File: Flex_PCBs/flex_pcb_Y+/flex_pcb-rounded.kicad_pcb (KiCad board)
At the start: 2 copper layers, 60 x 43.9 mm, 3 parts, among them J1 Conn_01x08_Male, J2 Conn_01x08_Male

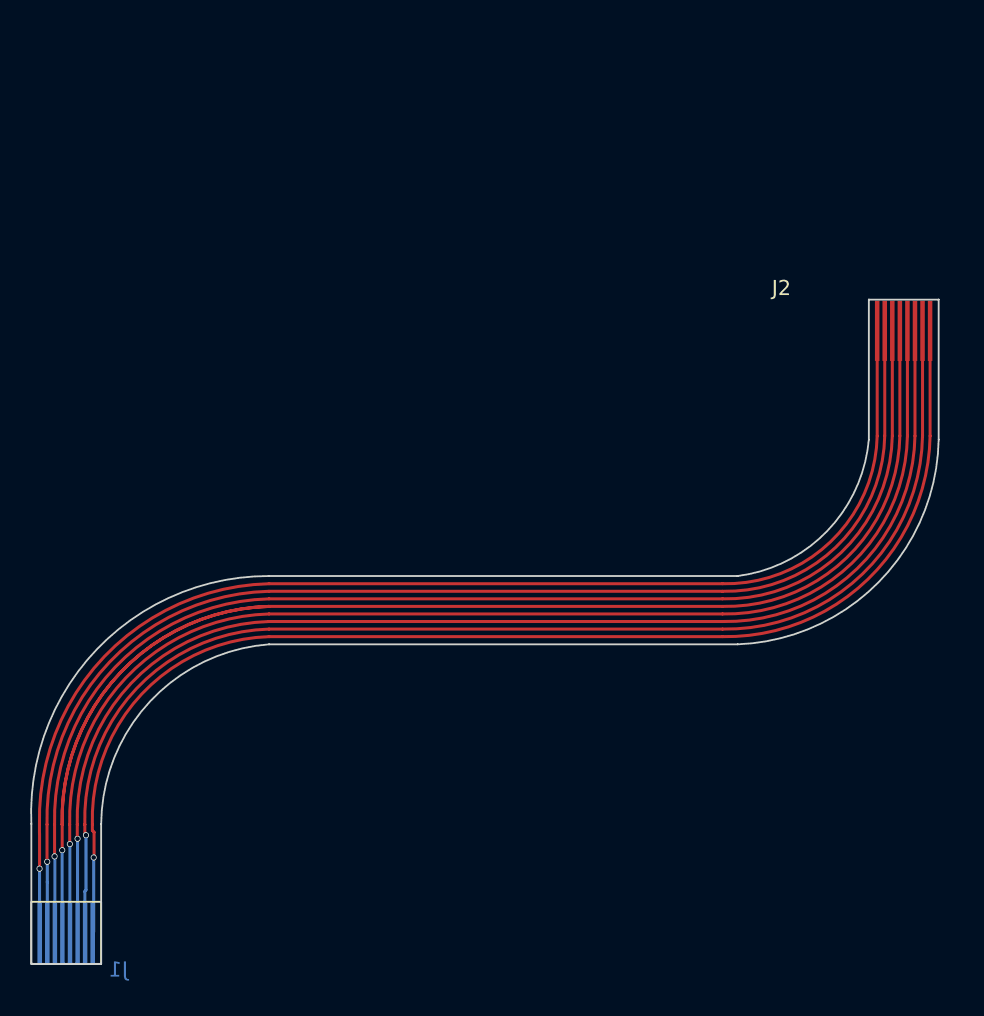
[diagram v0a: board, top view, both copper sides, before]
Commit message: Added small modifications to the existing flex PCBs plus the new ones: Y- and X-.
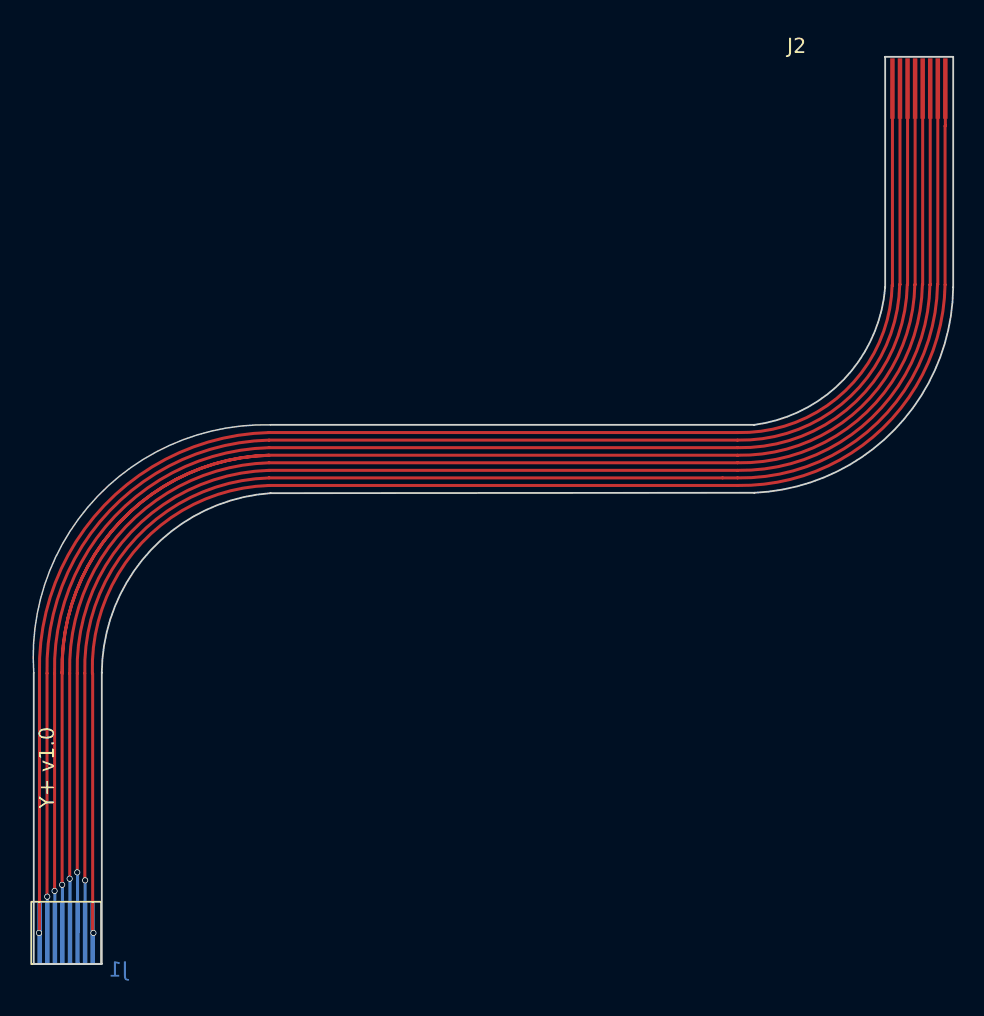
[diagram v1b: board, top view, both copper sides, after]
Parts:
- moved J2 16.1 mm to (166.7, 56.6)
- moved REF** 0.10 mm to (110.4, 112.5)
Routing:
- net 6: track 83.3 -> 100.3 mm
- net 8: track 83.4 -> 100.3 mm
- net 7: track 83.3 -> 100.3 mm
- net 4: track 105.4 -> 121.9 mm
- net 1: track 83.9 -> 100.4 mm
- net 5: track 83.9 -> 100.3 mm
- net 3: track 83.9 -> 100.3 mm
- net 2: track 83.9 -> 100.3 mm
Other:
- board size 60 x 43.9 mm -> 60.8 x 60 mm
- board text added: "The PCB should have a thickness of 0.12 mm (two Layer). On the marked areas in User.1 layer a 0.225 mm polyimide stiffener should be glued. The resulting gold fingers should have 0.3 mm in thickness."
- board text added: "Y+ v1.0"
- board text removed: "User.1 defined areas should have the 0.25 mm stiffeners on the opposite side of the pins."
